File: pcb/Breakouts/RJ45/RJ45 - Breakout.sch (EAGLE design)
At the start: 3 parts

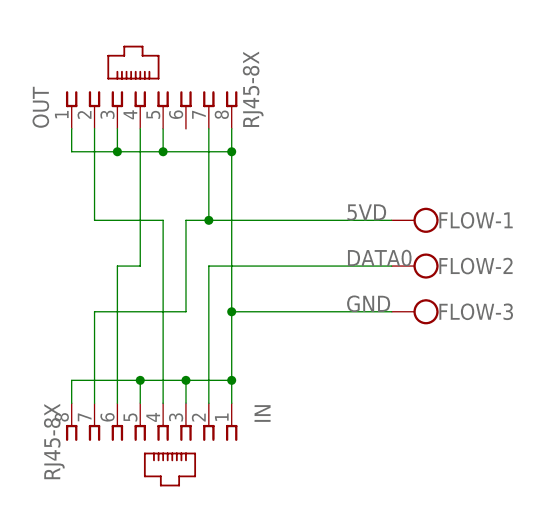
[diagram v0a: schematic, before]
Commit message: Rewire, move to 9 meters
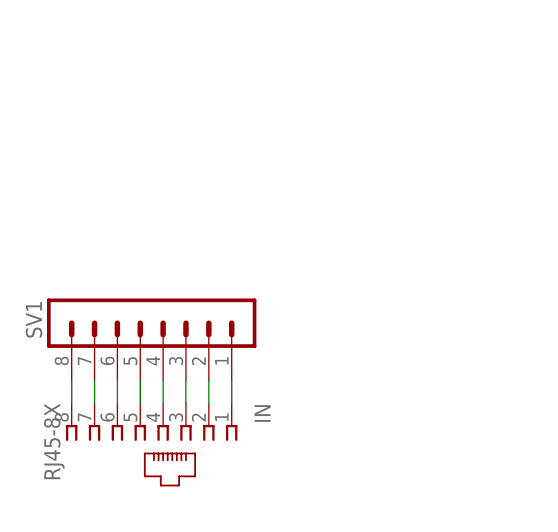
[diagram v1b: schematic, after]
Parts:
- removed FLOW: (no value), con-wago-500:W237-103
- removed OUT: RJ45-8X, con-tycoelectronics:RJ45-8X
- added SV1: (no value), con-lstb:MA08-1
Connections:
- removed net 5VD: FLOW-1.KL, IN.7, OUT.7
- removed net DATA0: FLOW-2.KL, IN.2
- removed net DATA1: IN.4, OUT.2
- removed net DATA2: IN.6, OUT.4
- removed net GND: FLOW-3.KL, IN.1, IN.3, IN.5, IN.8, OUT.1, OUT.3, OUT.5, OUT.8
- new net 1: IN.1, SV1.1
- new net 2: IN.2, SV1.2
- new net 3: IN.3, SV1.3
- new net 4: IN.4, SV1.4
- new net 5: IN.5, SV1.5
- new net 6: IN.6, SV1.6
- new net 7: IN.7, SV1.7
- new net 8: IN.8, SV1.8
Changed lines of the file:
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@@
 <parts>
 <part name="IN" library="con-tycoelectronics" library_urn="urn:adsk.eagle:library:193" deviceset="RJ45" device="" package3d_urn="urn:adsk.eagle:package:10660/1" technology="-8X"/>
-<part name="OUT" library="con-tycoelectronics" library_urn="urn:adsk.eagle:library:193" deviceset="RJ45" device="" package3d_urn="urn:adsk.eagle:package:10660/1" technology="-8X"/>
-<part name="FLOW" library="con-wago-500" library_urn="urn:adsk.eagle:library:195" deviceset="W237-103" device="" package3d_urn="urn:adsk.eagle:package:10691/1"/>
+<part name="SV1" library="con-lstb" library_urn="urn:adsk.eagle:library:162" deviceset="MA08-1" device="" package3d_urn="urn:adsk.eagle:package:8343/1"/>
 </parts>
 <sheets>
@@
 <attribute name="VALUE" x="50.292" y="35.56" size="1.778" layer="96" rot="R270"/>
 </instance>
-<instance part="OUT" gate="G$1" x="60.96" y="68.58" smashed="yes" rot="R90">
-<attribute name="NAME" x="50.8" y="66.04" size="1.778" layer="95" rot="R90"/>
-<attribute name="VALUE" x="74.168" y="66.04" size="1.778" layer="96" rot="R90"/>
-</instance>
-<instance part="FLOW" gate="-1" x="93.98" y="55.88" smashed="yes" rot="R180">
-<attribute name="NAME" x="93.98" y="54.991" size="1.778" layer="95"/>
-</instance>
-<instance part="FLOW" gate="-2" x="93.98" y="50.8" smashed="yes" rot="R180">
-<attribute name="NAME" x="93.98" y="49.911" size="1.778" layer="95"/>
-</instance>
-<instance part="FLOW" gate="-3" x="93.98" y="45.72" smashed="yes" rot="R180">
-<attribute name="VALUE" x="96.52" y="49.403" size="1.778" layer="96" rot="R180"/>
-<attribute name="NAME" x="93.98" y="44.831" size="1.778" layer="95"/>
+<instance part="SV1" gate="1" x="63.5" y="45.72" smashed="yes" rot="MR270">
+<attribute name="VALUE" x="76.2" y="46.99" size="1.778" layer="96" rot="MR270"/>
+<attribute name="NAME" x="50.038" y="46.99" size="1.778" layer="95" rot="MR270"/>
 </instance>
 </instances>
@@
 </busses>
 <nets>
-<net name="GND" class="0">
+<net name="8" class="0">
+<segment>
+<pinref part="IN" gate="G$1" pin="8"/>
+<pinref part="SV1" gate="1" pin="8"/>
+<wire x1="53.34" y1="35.56" x2="53.34" y2="38.1" width="0.1524" layer="91"/>
+</segment>
+</net>
+<net name="7" class="0">
+<segment>
+<pinref part="IN" gate="G$1" pin="7"/>
+<pinref part="SV1" gate="1" pin="7"/>
+<wire x1="55.88" y1="35.56" x2="55.88" y2="38.1" width="0.1524" layer="91"/>
+</segment>
+</net>
+<net name="6" class="0">
+<segment>
+<pinref part="IN" gate="G$1" pin="6"/>
+<pinref part="SV1" gate="1" pin="6"/>
+<wire x1="58.42" y1="35.56" x2="58.42" y2="38.1" width="0.1524" layer="91"/>
+</segment>
+</net>
+<net name="5" class="0">
+<segment>
+<pinref part="IN" gate="G$1" pin="5"/>
+<pinref part="SV1" gate="1" pin="5"/>
+<wire x1="60.96" y1="35.56" x2="60.96" y2="38.1" width="0.1524" layer="91"/>
+</segment>
+</net>
+<net name="4" class="0">
+<segment>
+<pinref part="IN" gate="G$1" pin="4"/>
+<pinref part="SV1" gate="1" pin="4"/>
+<wire x1="63.5" y1="35.56" x2="63.5" y2="38.1" width="0.1524" layer="91"/>
+</segment>
+</net>
+<net name="3" class="0">
+<segment>
+<pinref part="IN" gate="G$1" pin="3"/>
+<pinref part="SV1" gate="1" pin="3"/>
+<wire x1="66.04" y1="35.56" x2="66.04" y2="38.1" width="0.1524" layer="91"/>
+</segment>
+</net>
+<net name="2" class="0">
+<segment>
+<pinref part="IN" gate="G$1" pin="2"/>
+<pinref part="SV1" gate="1" pin="2"/>
+<wire x1="68.58" y1="35.56" x2="68.58" y2="38.1" width="0.1524" layer="91"/>
+</segment>
+</net>
+<net name="1" class="0">
 <segment>
 <pinref part="IN" gate="G$1" pin="1"/>
+<pinref part="SV1" gate="1" pin="1"/>
 <wire x1="71.12" y1="35.56" x2="71.12" y2="38.1" width="0.1524" layer="91"/>
-<wire x1="71.12" y1="38.1" x2="71.12" y2="45.72" width="0.1524" layer="91"/>
-<wire x1="71.12" y1="45.72" x2="71.12" y2="63.5" width="0.1524" layer="91"/>
-<wire x1="71.12" y1="38.1" x2="66.04" y2="38.1" width="0.1524" layer="91"/>
-<junction x="71.12" y="38.1"/>
-<pinref part="IN" gate="G$1" pin="3"/>
-<wire x1="66.04" y1="38.1" x2="66.04" y2="35.56" width="0.1524" layer="91"/>
-<wire x1="66.04" y1="38.1" x2="60.96" y2="38.1" width="0.1524" layer="91"/>
-<junction x="66.04" y="38.1"/>
-<pinref part="IN" gate="G$1" pin="5"/>
-<wire x1="60.96" y1="38.1" x2="60.96" y2="35.56" width="0.1524" layer="91"/>
-<pinref part="IN" gate="G$1" pin="8"/>
-<wire x1="53.34" y1="35.56" x2="53.34" y2="38.1" width="0.1524" layer="91"/>
-<wire x1="60.96" y1="38.1" x2="53.34" y2="38.1" width="0.1524" layer="91"/>
-<junction x="60.96" y="38.1"/>
-<pinref part="OUT" gate="G$1" pin="1"/>
-<wire x1="53.34" y1="66.04" x2="53.34" y2="63.5" width="0.1524" layer="91"/>
-<pinref part="OUT" gate="G$1" pin="8"/>
-<wire x1="71.12" y1="63.5" x2="71.12" y2="66.04" width="0.1524" layer="91"/>
-<pinref part="OUT" gate="G$1" pin="5"/>
-<wire x1="63.5" y1="63.5" x2="63.5" y2="66.04" width="0.1524" layer="91"/>
-<wire x1="63.5" y1="63.5" x2="71.12" y2="63.5" width="0.1524" layer="91"/>
-<junction x="63.5" y="63.5"/>
-<pinref part="OUT" gate="G$1" pin="3"/>
-<wire x1="58.42" y1="66.04" x2="58.42" y2="63.5" width="0.1524" layer="91"/>
-<wire x1="58.42" y1="63.5" x2="63.5" y2="63.5" width="0.1524" layer="91"/>
-<junction x="58.42" y="63.5"/>
-<wire x1="58.42" y1="63.5" x2="53.34" y2="63.5" width="0.1524" layer="91"/>
-<junction x="71.12" y="63.5"/>
-<pinref part="FLOW" gate="-3" pin="KL"/>
-<wire x1="88.9" y1="45.72" x2="71.12" y2="45.72" width="0.1524" layer="91"/>
-<junction x="71.12" y="45.72"/>
-<label x="83.82" y="45.72" size="1.778" layer="95"/>
 </segment>
 </net>
-<net name="DATA0" class="0">
-<segment>
-<pinref part="IN" gate="G$1" pin="2"/>
-<wire x1="68.58" y1="35.56" x2="68.58" y2="50.8" width="0.1524" layer="91"/>
-<pinref part="FLOW" gate="-2" pin="KL"/>
-<wire x1="68.58" y1="50.8" x2="88.9" y2="50.8" width="0.1524" layer="91"/>
-<label x="83.82" y="50.8" size="1.778" layer="95"/>
-</segment>
-</net>
-<net name="5VD" class="0">
-<segment>
-<pinref part="IN" gate="G$1" pin="7"/>
-<wire x1="55.88" y1="35.56" x2="55.88" y2="45.72" width="0.1524" layer="91"/>
-<wire x1="55.88" y1="45.72" x2="66.04" y2="45.72" width="0.1524" layer="91"/>
-<wire x1="66.04" y1="45.72" x2="66.04" y2="55.88" width="0.1524" layer="91"/>
-<wire x1="66.04" y1="55.88" x2="68.58" y2="55.88" width="0.1524" layer="91"/>
-<pinref part="OUT" gate="G$1" pin="7"/>
-<wire x1="68.58" y1="55.88" x2="68.58" y2="66.04" width="0.1524" layer="91"/>
-<pinref part="FLOW" gate="-1" pin="KL"/>
-<wire x1="88.9" y1="55.88" x2="68.58" y2="55.88" width="0.1524" layer="91"/>
-<junction x="68.58" y="55.88"/>
-<label x="83.82" y="55.88" size="1.778" layer="95"/>
-</segment>
-</net>
-<net name="DATA1" class="0">
-<segment>
-<pinref part="IN" gate="G$1" pin="4"/>
-<wire x1="63.5" y1="35.56" x2="63.5" y2="55.88" width="0.1524" layer="91"/>
-<pinref part="OUT" gate="G$1" pin="2"/>
-<wire x1="63.5" y1="55.88" x2="55.88" y2="55.88" width="0.1524" layer="91"/>
-<wire x1="55.88" y1="55.88" x2="55.88" y2="66.04" width="0.1524" layer="91"/>
-</segment>
-</net>
-<net name="DATA2" class="0">
-<segment>
-<pinref part="IN" gate="G$1" pin="6"/>
-<wire x1="58.42" y1="35.56" x2="58.42" y2="50.8" width="0.1524" layer="91"/>
-<wire x1="58.42" y1="50.8" x2="60.96" y2="50.8" width="0.1524" layer="91"/>
-<pinref part="OUT" gate="G$1" pin="4"/>
-<wire x1="60.96" y1="50.8" x2="60.96" y2="66.04" width="0.1524" layer="91"/>
-</segment>
-</net>
